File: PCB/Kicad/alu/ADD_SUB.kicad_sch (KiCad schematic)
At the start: 9 parts, among them U16 74LS283, U17 74LS283, U18 74LS283, U19 74LS283, U20 74LS86, U21 74LS86, U22 74LS86, U23 74LS86, U24 74LS86

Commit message: UPDATE
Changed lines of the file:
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@@
 	(paper "A4")
 	(no_connect
-		(at 236.22 127)
+		(at 232.41 127)
 	)
 	(no_connect
-		(at 246.38 127)
-	)
-	(no_connect
-		(at 266.7 127)
+		(at 242.57 127)
 	)
 	(no_connect
 		(at 256.54 127)
 	)
+	(no_connect
+		(at 252.73 127)
+	)
 	(wire
 		(pts
@@
 	(hierarchical_label "IS_SUB"
 		(shape input)
-		(at 256.54 127 180)
+		(at 252.73 127 180)
 		(effects
 			(font
@@
 	(hierarchical_label "B[0..15]"
 		(shape input)
-		(at 246.38 127 180)
+		(at 242.57 127 180)
 		(effects
 			(font
@@
 	(hierarchical_label "ADD_SUB[0..15]"
 		(shape output)
-		(at 266.7 127 0)
+		(at 256.54 127 0)
 		(effects
 			(font
@@
 	(hierarchical_label "A[0..15]"
 		(shape input)
-		(at 236.22 127 180)
-		(effects
-			(font
+		(at 232.41 127 180)
+		(effects
+			(font

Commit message: UPDATE
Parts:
- added C17, C18, C19, C20, C21, C66, C67, C68, C69: 10n, symbol Device:C
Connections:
- net GND: now also C17.2, C18.2, C19.2, C20.2, C21.2, C66.2, C67.2, C68.2, C69.2
- net VCC: now also C17.1, C18.1, C19.1, C20.1, C21.1, C66.1, C67.1, C68.1, C69.1
- net C0 renamed COUT0
- net C1 renamed COUT1
- net C2 renamed COUT2
- net C3 renamed FC
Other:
- moved on the sheet: U17, U19, U20E, U21A, U21B, U21C, U21D, U21E, U22E, U23A, U23B, U23C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

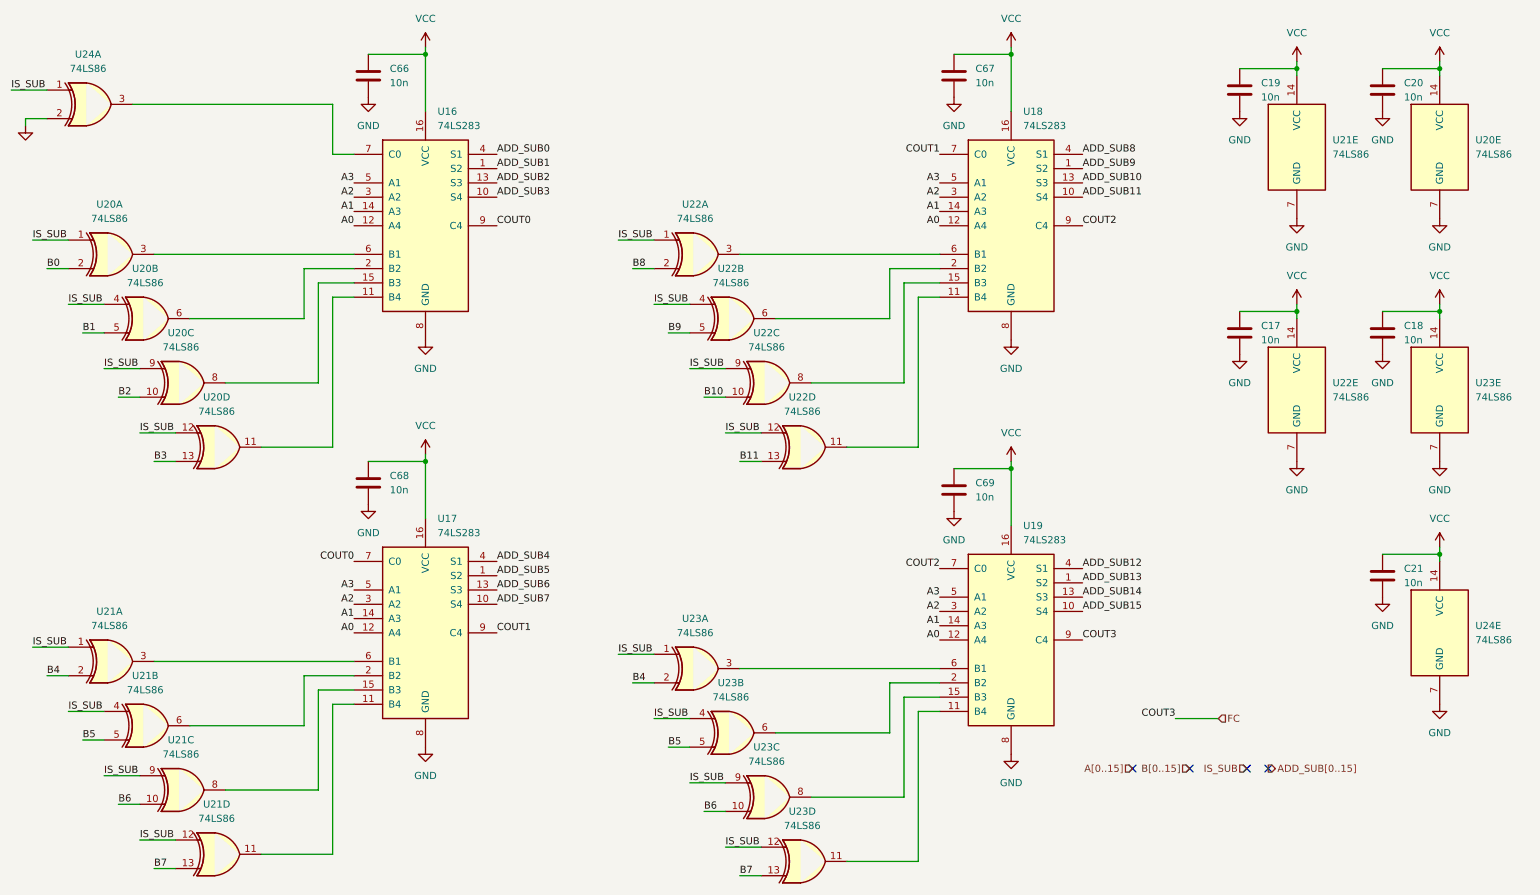
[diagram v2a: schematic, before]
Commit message: LEDs added
REGISTER.kicad_sch LEDs added to both REG_A and REG_B
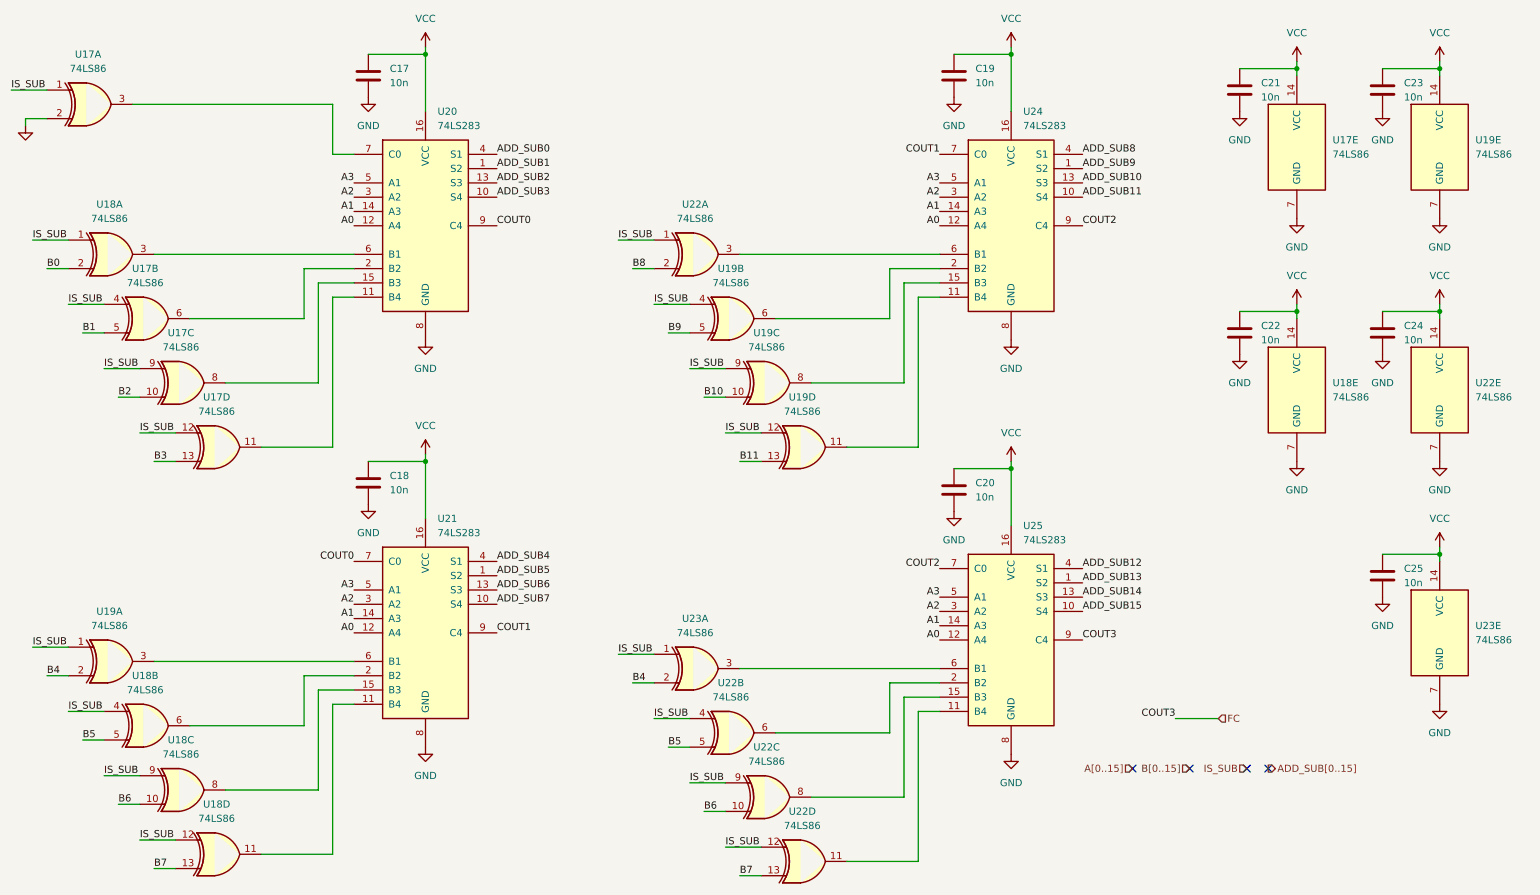
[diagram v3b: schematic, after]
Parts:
- renumbered C66 to C17, C68 to C18, C67 to C19, C69 to C20, C19 to C21, C17 to C22, C20 to C23, C18 to C24, C21 to C25, U20 to U17, U21 to U17, U24 to U17, U21 to U18, U20 to U18, U22 to U18, U22 to U19, U21 to U19, U20 to U19, U16 to U20, U17 to U21, U23 to U22, U24 to U23, U18 to U24, U19 to U25

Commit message: Footprints, PCB update
Added footprints to all components, updated the PCB with the schematic
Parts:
- C17, C18, C19, C20, C21, C22, C23, C24, C25: footprint (none) -> Capacitor_SMD:C_0603_1608Metric
- U17, U18, U19, U22, U23: footprint (none) -> Package_SO:SOIC-14_3.9x8.7mm_P1.27mm
- U20, U21, U24, U25: footprint (none) -> Package_SO:SOIC-16_3.9x9.9mm_P1.27mm
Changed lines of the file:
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@@
 			)
 		)
-		(property "Footprint" ""
+		(property "Footprint" "Package_SO:SOIC-14_3.9x8.7mm_P1.27mm"
 			(at 40.64 140.97 0)
 			(effects
@@
 			)
 		)
-		(property "Footprint" ""
+		(property "Footprint" "Package_SO:SOIC-16_3.9x9.9mm_P1.27mm"
 			(at 194.31 125.73 0)
 			(effects
@@
 			)
 		)
-		(property "Footprint" ""
+		(property "Footprint" "Package_SO:SOIC-14_3.9x8.7mm_P1.27mm"
 			(at 138.43 57.15 0)
 			(effects
@@
 			)
 		)
-		(property "Footprint" ""
+		(property "Footprint" "Package_SO:SOIC-14_3.9x8.7mm_P1.27mm"
 			(at 151.13 80.01 0)
 			(effects
@@
 			)
 		)
-		(property "Footprint" ""
+		(property "Footprint" "Capacitor_SMD:C_0603_1608Metric"
 			(at 185.1152 102.87 0)
 			(effects
@@
 			)
 		)
-		(property "Footprint" ""
+		(property "Footprint" "Capacitor_SMD:C_0603_1608Metric"
 			(at 185.1152 29.21 0)
 			(effects
@@
 			)
 		)
-		(property "Footprint" ""
+		(property "Footprint" "Capacitor_SMD:C_0603_1608Metric"
 			(at 261.3152 118.11 0)
 			(effects
@@
 			)
 		)
-		(property "Footprint" ""
+		(property "Footprint" "Package_SO:SOIC-14_3.9x8.7mm_P1.27mm"
 			(at 46.99 152.4 0)
 			(effects
@@
 			)
 		)
-		(property "Footprint" ""
+		(property "Footprint" "Package_SO:SOIC-14_3.9x8.7mm_P1.27mm"
 			(at 53.34 163.83 0)
 			(effects
@@
 			)
 		)
-		(property "Footprint" ""
+		(property "Footprint" "Package_SO:SOIC-14_3.9x8.7mm_P1.27mm"
 			(at 270.51 81.28 0)
 			(effects
@@
 			)
 		)
-		(property "Footprint" ""
+		(property "Footprint" "Package_SO:SOIC-16_3.9x9.9mm_P1.27mm"
 			(at 194.31 52.07 0)
 			(effects
@@
 			)
 		)
-		(property "Footprint" ""
+		(property "Footprint" "Package_SO:SOIC-14_3.9x8.7mm_P1.27mm"
 			(at 157.48 91.44 0)
 			(effects
@@
 			)
 		)
-		(property "Footprint" ""
+		(property "Footprint" "Package_SO:SOIC-14_3.9x8.7mm_P1.27mm"
 			(at 270.51 124.46 0)
 			(effects
@@
 			)
 		)
-		(property "Footprint" ""
+		(property "Footprint" "Package_SO:SOIC-16_3.9x9.9mm_P1.27mm"
 			(at 90.17 52.07 0)
 			(effects
@@
 			)
 		)
-		(property "Footprint" ""
+		(property "Footprint" "Package_SO:SOIC-14_3.9x8.7mm_P1.27mm"
 			(at 138.43 130.81 0)
 			(effects
@@
 			)
 		)
-		(property "Footprint" ""
+		(property "Footprint" "Package_SO:SOIC-16_3.9x9.9mm_P1.27mm"
 			(at 90.17 124.46 0)
 			(effects
@@
 			)
 		)
-		(property "Footprint" ""
+		(property "Footprint" "Package_SO:SOIC-14_3.9x8.7mm_P1.27mm"
 			(at 144.78 68.58 0)
 			(effects
@@
 			)
 		)
-		(property "Footprint" ""
+		(property "Footprint" "Package_SO:SOIC-14_3.9x8.7mm_P1.27mm"
 			(at 46.99 80.01 0)
 			(effects
@@
 			)
 		)
-		(property "Footprint" ""
+		(property "Footprint" "Capacitor_SMD:C_0603_1608Metric"
 			(at 80.9752 101.6 0)
 			(effects
@@
 			)
 		)
-		(property "Footprint" ""
+		(property "Footprint" "Package_SO:SOIC-14_3.9x8.7mm_P1.27mm"
 			(at 151.13 153.67 0)
 			(effects
@@
 			)
 		)
-		(property "Footprint" ""
+		(property "Footprint" "Capacitor_SMD:C_0603_1608Metric"
 			(at 235.9152 74.93 0)
 			(effects
@@
 			)
 		)
-		(property "Footprint" ""
+		(property "Footprint" "Package_SO:SOIC-14_3.9x8.7mm_P1.27mm"
 			(at 40.64 68.58 0)
 			(effects
@@
 			)
 		)
-		(property "Footprint" ""
+		(property "Footprint" "Package_SO:SOIC-14_3.9x8.7mm_P1.27mm"
 			(at 34.29 129.54 0)
 			(effects
@@
 			)
 		)
-		(property "Footprint" ""
+		(property "Footprint" "Package_SO:SOIC-14_3.9x8.7mm_P1.27mm"
 			(at 34.29 57.15 0)
 			(effects
@@
 			)
 		)
-		(property "Footprint" ""
+		(property "Footprint" "Package_SO:SOIC-14_3.9x8.7mm_P1.27mm"
 			(at 245.11 38.1 0)
 			(effects
@@
 			)
 		)
-		(property "Footprint" ""
+		(property "Footprint" "Capacitor_SMD:C_0603_1608Metric"
 			(at 80.9752 29.21 0)
 			(effects
@@
 			)
 		)
-		(property "Footprint" ""
+		(property "Footprint" "Package_SO:SOIC-14_3.9x8.7mm_P1.27mm"
 			(at 53.34 91.44 0)
 			(effects
@@
 			)
 		)
-		(property "Footprint" ""
+		(property "Footprint" "Package_SO:SOIC-14_3.9x8.7mm_P1.27mm"
 			(at 30.48 30.48 0)
 			(effects
@@
 			)
 		)
-		(property "Footprint" ""
+		(property "Footprint" "Package_SO:SOIC-14_3.9x8.7mm_P1.27mm"
 			(at 144.78 142.24 0)
 			(effects
@@
 			)
 		)
-		(property "Footprint" ""
+		(property "Footprint" "Capacitor_SMD:C_0603_1608Metric"
 			(at 261.3152 74.93 0)
 			(effects
@@
 			)
 		)
-		(property "Footprint" ""
+		(property "Footprint" "Package_SO:SOIC-14_3.9x8.7mm_P1.27mm"
 			(at 270.51 38.1 0)
 			(effects
@@
 			)
 		)
-		(property "Footprint" ""
+		(property "Footprint" "Capacitor_SMD:C_0603_1608Metric"
 			(at 235.9152 31.75 0)
 			(effects
@@
 			)
 		)
-		(property "Footprint" ""
+		(property "Footprint" "Capacitor_SMD:C_0603_1608Metric"
 			(at 261.3152 31.75 0)
 			(effects
@@
 			)
 		)
-		(property "Footprint" ""
+		(property "Footprint" "Package_SO:SOIC-14_3.9x8.7mm_P1.27mm"
 			(at 157.48 165.1 0)
 			(effects
@@
 			)
 		)
-		(property "Footprint" ""
+		(property "Footprint" "Package_SO:SOIC-14_3.9x8.7mm_P1.27mm"
 			(at 245.11 81.28 0)
 			(effects

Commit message: ALU Pcb update
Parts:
- C17, C18, C19, C20, C21, C22, C23, C24, C25: value 10n -> 100nF; footprint Capacitor_SMD:C_0603_1608Metric -> Capacitor_SMD:C_0402_1005Metric
- U17, U18, U19, U22, U23: value 74LS86 -> 7486; footprint Package_SO:SOIC-14_3.9x8.7mm_P1.27mm -> Package_SO:SO-14_3.9x8.65mm_P1.27mm
- U20, U21, U24, U25: value 74LS283 -> 74283

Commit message: PCB
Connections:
- net A0: no longer U21.12 (A4), U24.12 (A4), U25.12 (A4)
- net A1: no longer U21.14 (A3), U24.14 (A3), U25.14 (A3)
- net A2: no longer U21.3 (A2), U24.3 (A2), U25.3 (A2)
- net A3: no longer U21.5 (A1), U24.5 (A1), U25.5 (A1)
- new net A10: U24.3 (A2)
- new net A11: U24.5 (A1)
- new net A12: U25.12 (A4)
- new net A13: U25.14 (A3)
- new net A14: U25.3 (A2)
- new net A15: U25.5 (A1)
- new net A4: U21.12 (A4)
- new net A5: U21.14 (A3)
- new net A6: U21.3 (A2)
- new net A7: U21.5 (A1)
- new net A8: U24.12 (A4)
- new net A9: U24.14 (A3)
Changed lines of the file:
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@@
 		)
 	)
-	(label "A2"
+	(label "A6"
 		(at 77.47 119.38 180)
 		(effects
@@
 		)
 	)
-	(label "A0"
+	(label "A12"
 		(at 181.61 125.73 180)
 		(effects
@@
 		)
 	)
-	(label "A1"
+	(label "A9"
 		(at 181.61 49.53 180)
 		(effects
@@
 		)
 	)
-	(label "A3"
+	(label "A15"
 		(at 181.61 118.11 180)
 		(effects
@@
 		)
 	)
-	(label "A3"
+	(label "A11"
 		(at 181.61 44.45 180)
 		(effects
@@
 		)
 	)
-	(label "A2"
+	(label "A10"
 		(at 181.61 46.99 180)
 		(effects
@@
 		)
 	)
-	(label "A1"
+	(label "A5"
 		(at 77.47 121.92 180)
 		(effects
@@
 		)
 	)
-	(label "A0"
+	(label "A4"
 		(at 77.47 124.46 180)
 		(effects
@@
 		)
 	)
-	(label "A3"
+	(label "A7"
 		(at 77.47 116.84 180)
 		(effects
@@
 		)
 	)
-	(label "A2"
+	(label "A14"
 		(at 181.61 120.65 180)
 		(effects
@@
 		)
 	)
-	(label "A0"
+	(label "A8"
 		(at 181.61 52.07 180)
 		(effects
@@
 		)
 	)
-	(label "A1"
+	(label "A13"
 		(at 181.61 123.19 180)
 		(effects

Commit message: Stuff and layout
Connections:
- net A10 is gone; now on net A2: U24.3 (A2)
- net A11 is gone; now on net A3: U24.5 (A1)
- net A12 is gone; now on net A0: U25.12 (A4)
- net A13 is gone; now on net A1: U25.14 (A3)
- net A14 is gone; now on net A2: U25.3 (A2)
- net A15 is gone; now on net A3: U25.5 (A1)
- net A4 is gone; now on net A0: U21.12 (A4)
- net A5 is gone; now on net A1: U21.14 (A3)
- net A6 is gone; now on net A2: U21.3 (A2)
- net A7 is gone; now on net A3: U21.5 (A1)
- net A8 is gone; now on net A0: U24.12 (A4)
- net A9 is gone; now on net A1: U24.14 (A3)
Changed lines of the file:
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@@
 		)
 	)
-	(label "A6"
+	(label "A2"
 		(at 77.47 119.38 180)
 		(effects
@@
 		)
 	)
-	(label "A12"
+	(label "A0"
 		(at 181.61 125.73 180)
 		(effects
@@
 		)
 	)
-	(label "A9"
+	(label "A1"
 		(at 181.61 49.53 180)
 		(effects
@@
 		)
 	)
-	(label "A15"
+	(label "A3"
 		(at 181.61 118.11 180)
 		(effects
@@
 		)
 	)
-	(label "A11"
+	(label "A3"
 		(at 181.61 44.45 180)
 		(effects
@@
 		)
 	)
-	(label "A10"
+	(label "A2"
 		(at 181.61 46.99 180)
 		(effects
@@
 		)
 	)
-	(label "A5"
+	(label "A1"
 		(at 77.47 121.92 180)
 		(effects
@@
 		)
 	)
-	(label "A4"
+	(label "A0"
 		(at 77.47 124.46 180)
 		(effects
@@
 		)
 	)
-	(label "A7"
+	(label "A3"
 		(at 77.47 116.84 180)
 		(effects
@@
 		)
 	)
-	(label "A14"
+	(label "A2"
 		(at 181.61 120.65 180)
 		(effects
@@
 		)
 	)
-	(label "A8"
+	(label "A0"
 		(at 181.61 52.07 180)
 		(effects
@@
 		)
 	)
-	(label "A13"
+	(label "A1"
 		(at 181.61 123.19 180)
 		(effects
